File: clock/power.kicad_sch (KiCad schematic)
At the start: 54 parts, among them Q501 BSS138, Q502 BSS138, U501 TPS56428, U502 TPS56428, U503 TPS56428

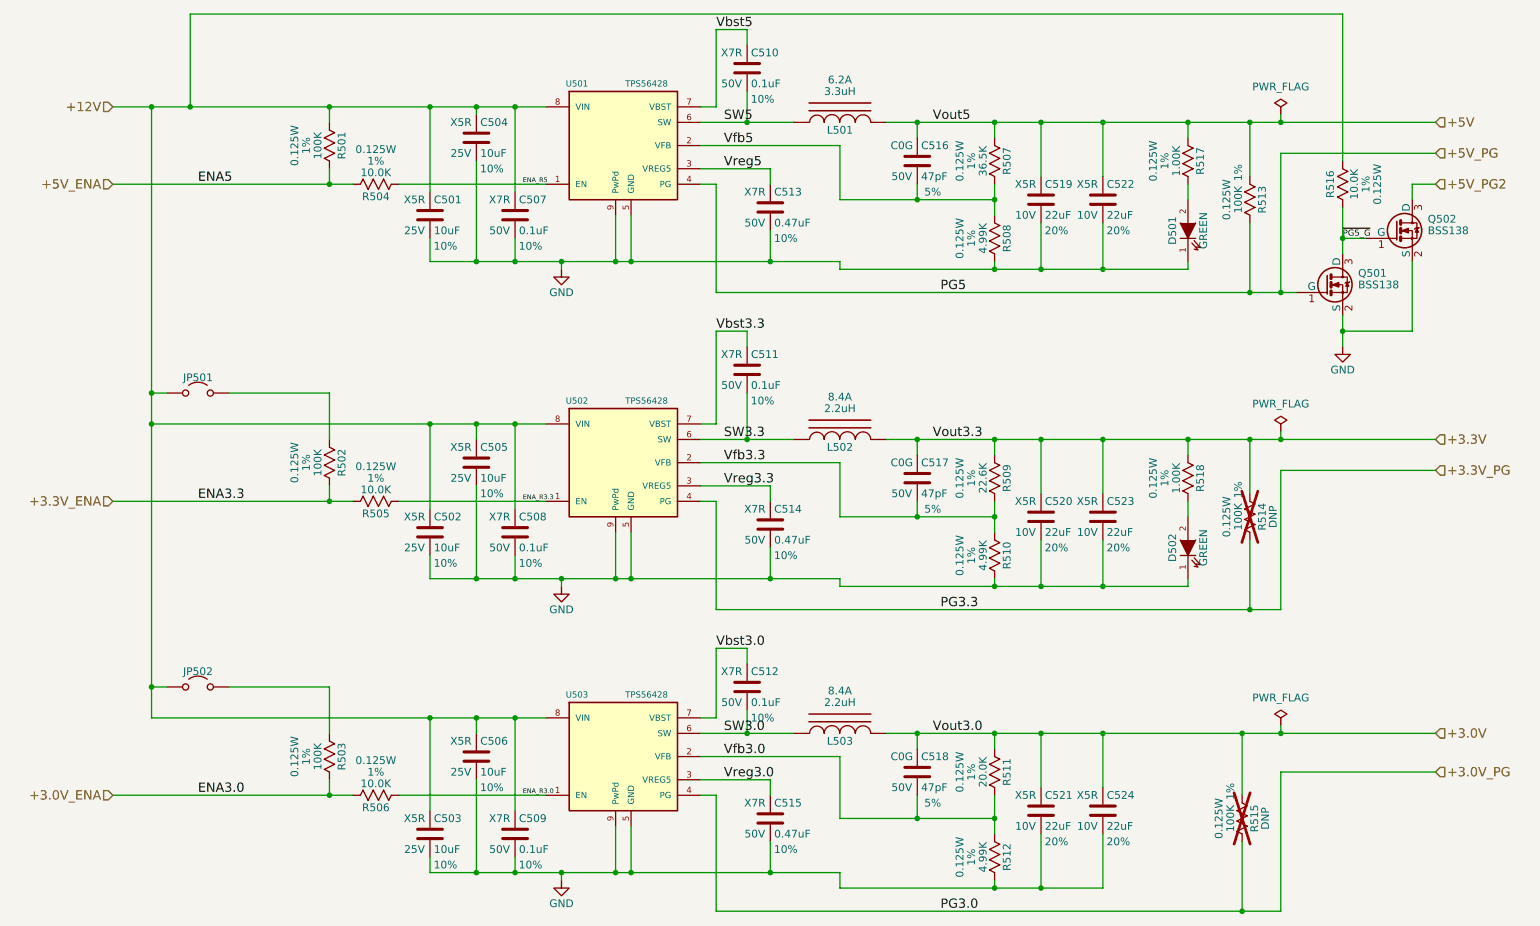
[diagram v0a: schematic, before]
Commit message: Make some net names consistent with hierarchy names. Clean up some silkscreen DRCs.
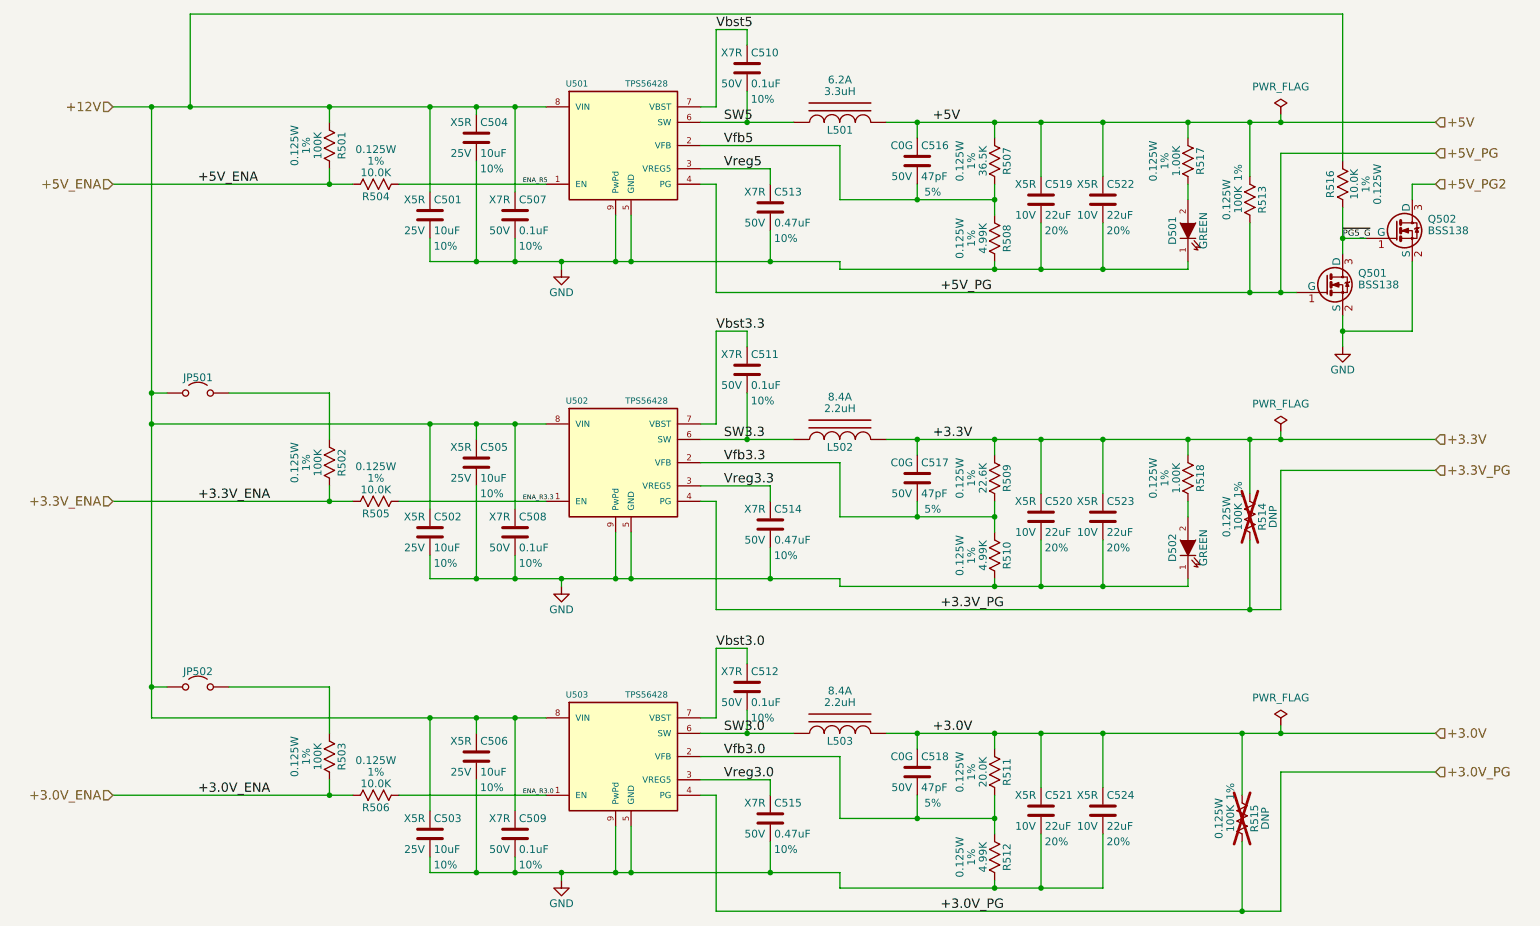
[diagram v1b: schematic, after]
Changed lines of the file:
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@@
 		)
 	)
-	(label "PG5"
+	(label "+5V_PG"
 		(at 166.37 60.96 0)
 		(fields_autoplaced yes)
@@
 		)
 	)
-	(label "PG3.3"
+	(label "+3.3V_PG"
 		(at 166.37 113.03 0)
 		(fields_autoplaced yes)
@@
 		)
 	)
-	(label "PG3.0"
+	(label "+3.0V_PG"
 		(at 166.37 162.56 0)
 		(fields_autoplaced yes)
@@
 		)
 	)
-	(label "Vout3.0"
+	(label "+3.0V"
 		(at 165.1 133.35 0)
 		(fields_autoplaced yes)
@@
 		)
 	)
-	(label "Vout3.3"
+	(label "+3.3V"
 		(at 165.1 85.09 0)
 		(fields_autoplaced yes)
@@
 		)
 	)
-	(label "Vout5"
+	(label "+5V"
 		(at 165.1 33.02 0)
 		(fields_autoplaced yes)
@@
 		)
 	)
-	(label "ENA3.3"
+	(label "+3.3V_ENA"
 		(at 44.45 95.25 0)
 		(fields_autoplaced yes)
@@
 		)
 	)
-	(label "ENA5"
+	(label "+5V_ENA"
 		(at 44.45 43.18 0)
 		(fields_autoplaced yes)
@@
 		)
 	)
-	(label "ENA3.0"
+	(label "+3.0V_ENA"
 		(at 44.45 143.51 0)
 		(fields_autoplaced yes)
